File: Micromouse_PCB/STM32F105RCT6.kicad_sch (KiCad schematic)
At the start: 12 parts, among them J3 ARM Cortex Debug, U1 STM32F105RCT6, Y1 8MHz, OT32258MJBA4SL

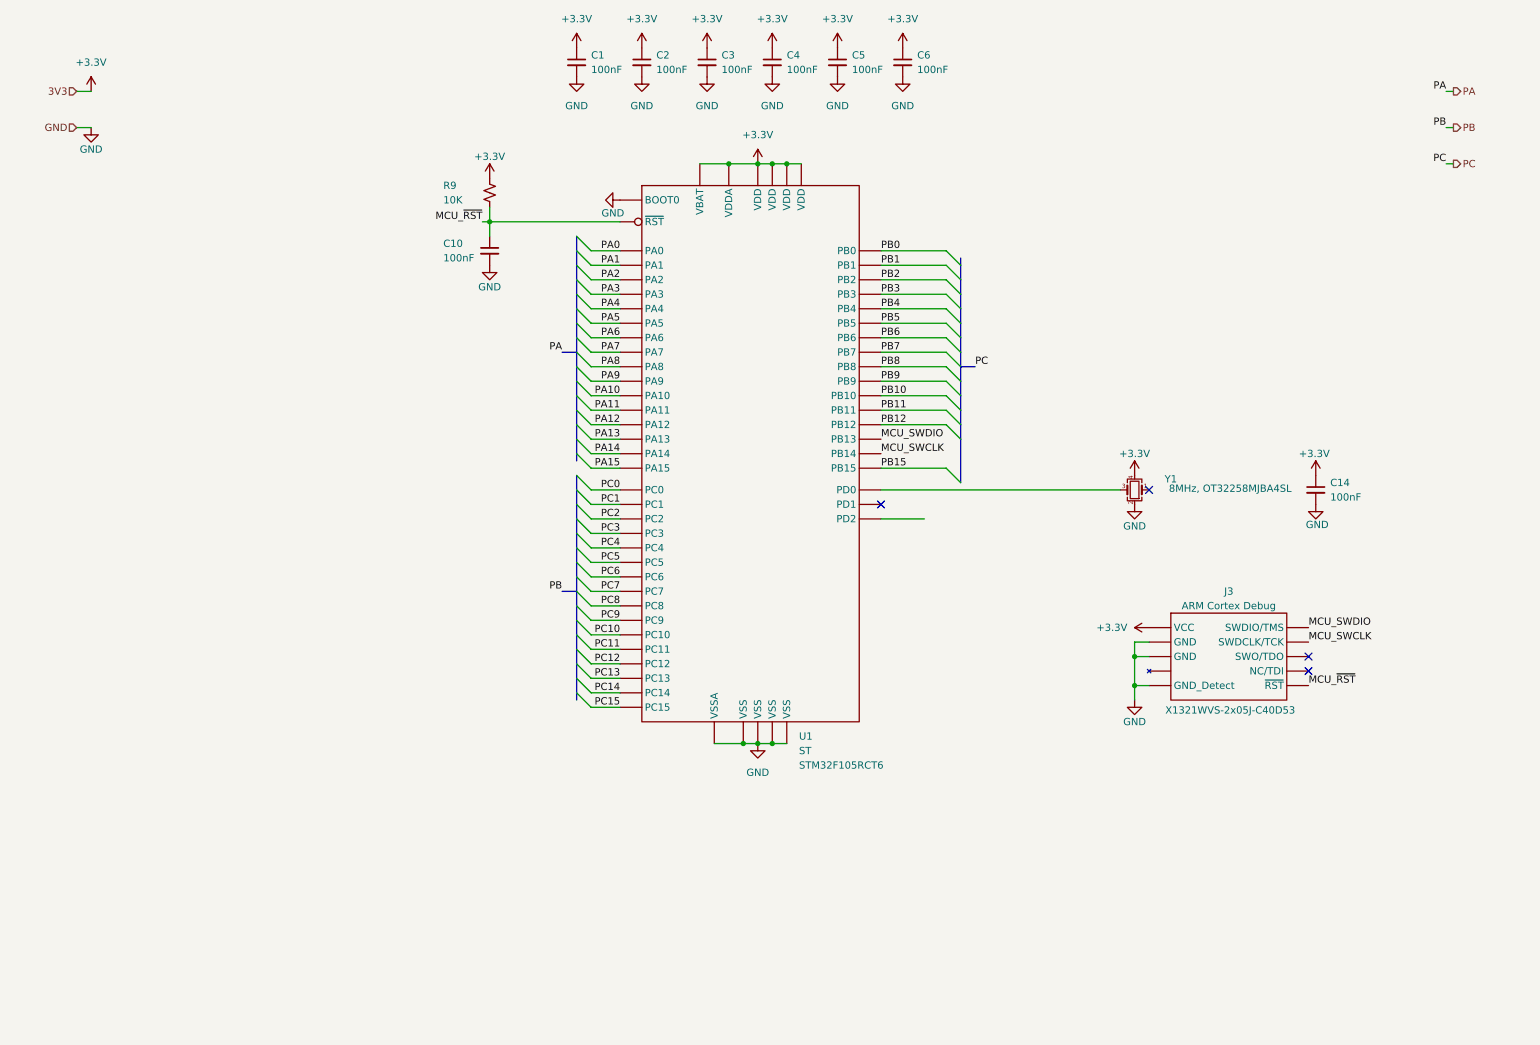
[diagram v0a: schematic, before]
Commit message: Schematic done
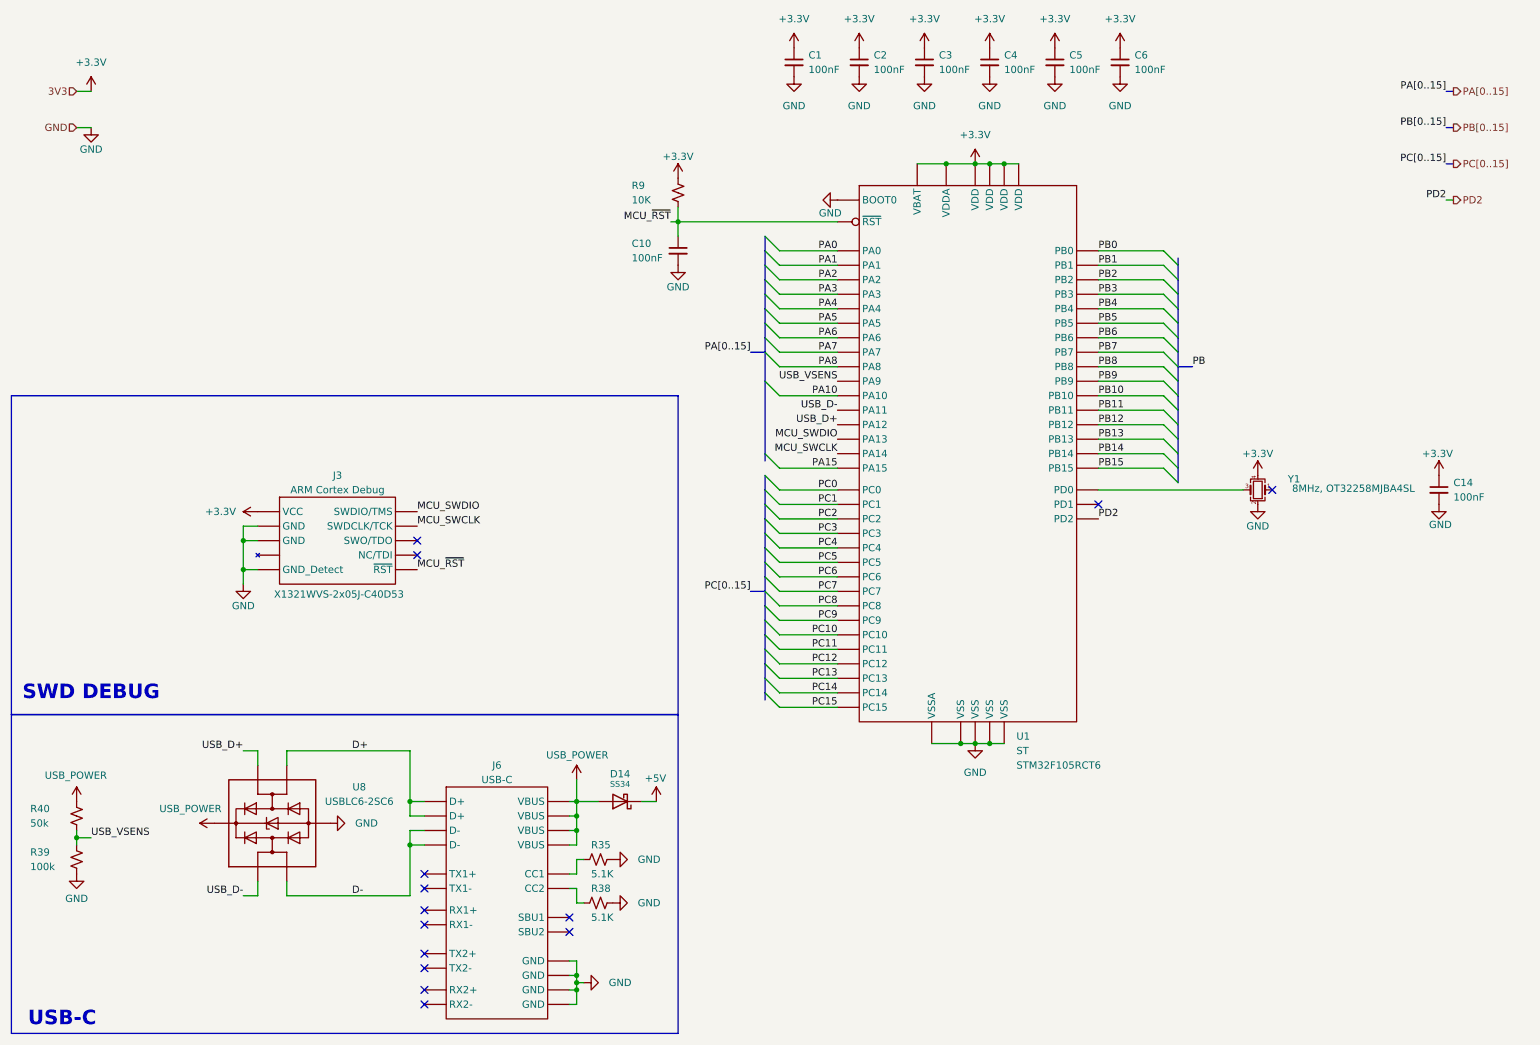
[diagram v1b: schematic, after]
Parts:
- added D14: SS34, Diode_SMD:D_SMA, symbol Diode:SS34
- added J6: USB-C, Connector_USB:USB_C_Receptacle_GCT_USB4105-xx-A_16P_TopMnt_Horizontal, symbol UCIRP-KiCAD-Lib:USB-C
- added R35, R38: 5.1K, Resistor_SMD:R_0603_1608Metric, symbol UCIRP-KiCAD-Lib:R_Small_US
- added R39: 100k, Resistor_SMD:R_0603_1608Metric, symbol Device:R_Small_US
- added R40: 50k, Resistor_SMD:R_0603_1608Metric, symbol Device:R_Small_US
- added U8: USBLC6-2SC6, Package_TO_SOT_SMD:SOT-23-6, symbol Power_Protection:USBLC6-2SC6
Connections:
- net PA13 is gone; now on net MCU_SWDIO: U1.46 (PA13)
- net PA14 is gone; now on net MCU_SWCLK: U1.49 (PA14)
- net GND: now also J6.A1 (GND), J6.A12 (GND), J6.B1 (GND), J6.B12 (GND), R35.1, R38.1, R39.1, U8.2 (GND)
- net MCU_SWCLK: no longer U1.35 (PB14)
- net MCU_SWDIO: no longer U1.34 (PB13)
- net PD2: now reaches U1.54 (PD2)
- net PA11 renamed USB_D-
- net USB_D-: now also U8.6 (I/O1)
- net PA12 renamed USB_D+
- net USB_D+: now also U8.4 (I/O2)
- net PA9 renamed USB_VSENS
- net USB_VSENS: now also R39.2, R40.1
- new net: J6.B5 (CC2), R38.2
- new net: J6.A5 (CC1), R35.2
- new net +5V: D14.1 (K)
- new net D+: J6.A6 (D+), J6.B6 (D+), U8.3 (I/O2)
- new net D-: J6.A7 (D-), J6.B7 (D-), U8.1 (I/O1)
- new net PB13: U1.34 (PB13)
- new net PB14: U1.35 (PB14)
- new net USB_POWER: D14.2 (A), J6.A4 (VBUS), J6.A9 (VBUS), J6.B4 (VBUS), J6.B9 (VBUS), R40.2, U8.5 (VBUS)
- no-connect marks 4 -> 14
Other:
- note added: "SWD DEBUG"
- note added: "USB-C"
- moved on the sheet: C1, C10, C14, C2, C3, C4, C5, C6, J3, R9, U1, Y1

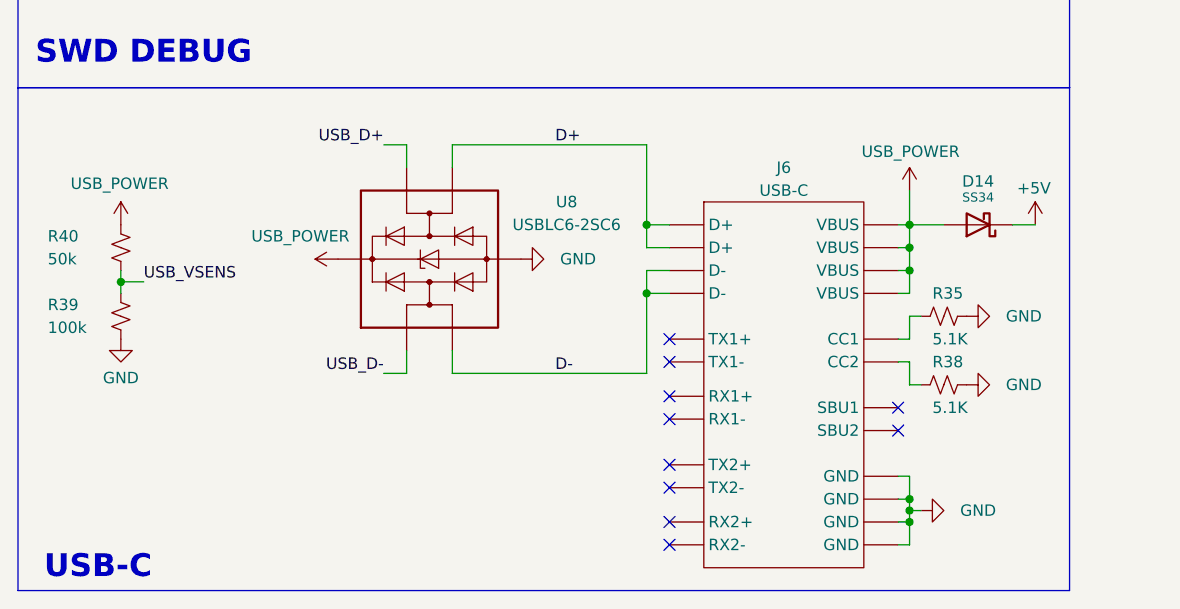
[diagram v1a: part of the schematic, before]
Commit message: Placement 75% done on PCB
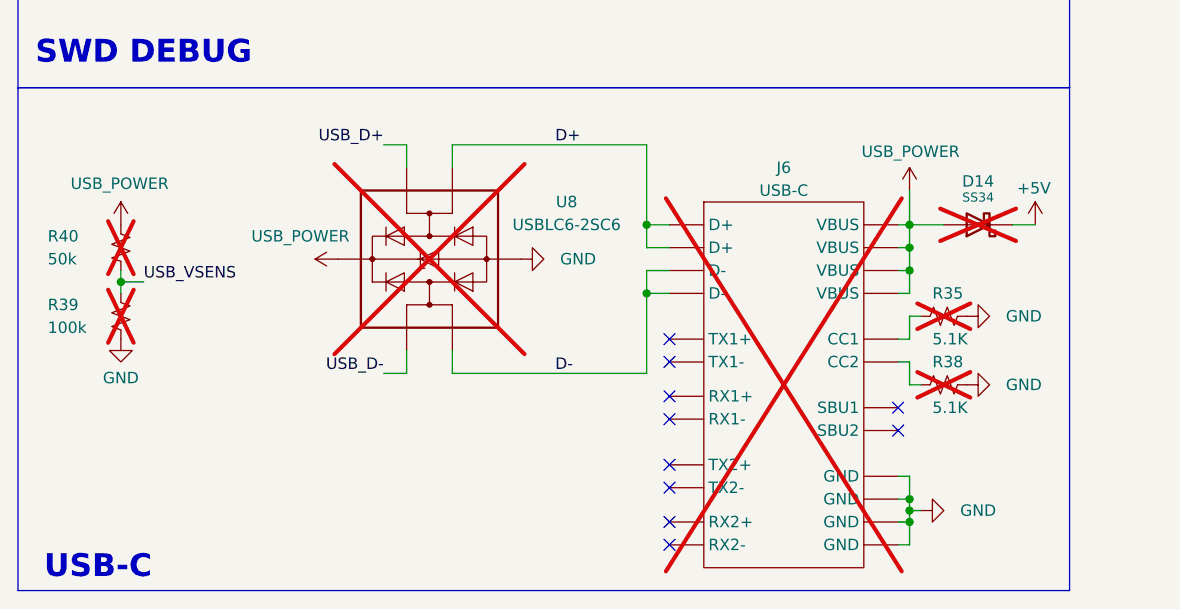
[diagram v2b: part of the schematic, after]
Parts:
- D14, J6, R35, R38, R39, R40, U8: now not fitted
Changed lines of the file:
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@@
 		(exclude_from_sim no)
 		(in_bom yes)
-		(on_board yes)
-		(dnp no)
+		(on_board no)
+		(dnp yes)
 		(property "Reference" "R40"
 			(at 17.272 157.48 0)
@@
 		(exclude_from_sim no)
 		(in_bom yes)
-		(on_board yes)
-		(dnp no)
+		(on_board no)
+		(dnp yes)
 		(property "Reference" "R38"
 			(at 115.57 171.45 90)
@@
 		(exclude_from_sim no)
 		(in_bom yes)
-		(on_board yes)
-		(dnp no)
+		(on_board no)
+		(dnp yes)
 		(property "Reference" "U8"
 			(at 74.93 153.67 90)
@@
 		(exclude_from_sim no)
 		(in_bom yes)
-		(on_board yes)
-		(dnp no)
+		(on_board no)
+		(dnp yes)
 		(property "Reference" "R39"
 			(at 17.272 165.1 0)
@@
 		(exclude_from_sim no)
 		(in_bom yes)
-		(on_board yes)
-		(dnp no)
+		(on_board no)
+		(dnp yes)
 		(property "Reference" "D14"
 			(at 120.65 151.384 0)
@@
 		(exclude_from_sim no)
 		(in_bom yes)
-		(on_board yes)
-		(dnp no)
+		(on_board no)
+		(dnp yes)
 		(property "Reference" "J6"
 			(at 99.06 149.86 0)
@@
 		(exclude_from_sim no)
 		(in_bom yes)
-		(on_board yes)
-		(dnp no)
+		(on_board no)
+		(dnp yes)
 		(property "Reference" "R35"
 			(at 115.57 163.83 90)

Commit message: PCB Done, need review now
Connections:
- net +3.3V renamed 3V3

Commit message: Ordered
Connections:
- net 3V3 renamed +3V3
